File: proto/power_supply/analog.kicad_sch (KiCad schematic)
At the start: 28 parts, among them U401 TSV914, U409 TSV914

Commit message: Finish alim sch, start PCB
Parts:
- renumbered U409 to U401, U401 to U402
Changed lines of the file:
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@@
   (symbol (lib_id "Amplifier_Operational:TSV914") (at 49.53 114.3 0) (unit 1)
     (in_bom yes) (on_board yes) (dnp no) (fields_autoplaced)
-    (property "Reference" "U409" (at 49.53 105.41 0)
+    (property "Reference" "U401" (at 49.53 105.41 0)
       (effects (font (size 1.27 1.27)))
     )
@@
       (project "power_supply"
         (path "/e87df9ac-84db-475c-955a-f1fa477bbb69/9874073e-3ac1-4f88-b38b-85e528930503"
-          (reference "U409") (unit 1)
+          (reference "U401") (unit 1)
         )
       )
@@
   (symbol (lib_id "Amplifier_Operational:TSV914") (at 100.33 114.3 0) (unit 4)
     (in_bom yes) (on_board yes) (dnp no)
-    (property "Reference" "U409" (at 100.33 104.775 0)
+    (property "Reference" "U401" (at 100.33 104.775 0)
       (effects (font (size 1.27 1.27)))
     )
@@
       (project "power_supply"
         (path "/e87df9ac-84db-475c-955a-f1fa477bbb69/9874073e-3ac1-4f88-b38b-85e528930503"
-          (reference "U409") (unit 4)
+          (reference "U401") (unit 4)
         )
       )
@@
   (symbol (lib_id "Amplifier_Operational:TSV914") (at 187.96 114.3 0) (unit 2)
     (in_bom yes) (on_board yes) (dnp no) (fields_autoplaced)
-    (property "Reference" "U401" (at 187.96 105.41 0)
+    (property "Reference" "U402" (at 187.96 105.41 0)
       (effects (font (size 1.27 1.27)))
     )
@@
       (project "power_supply"
         (path "/e87df9ac-84db-475c-955a-f1fa477bbb69/9874073e-3ac1-4f88-b38b-85e528930503"
-          (reference "U401") (unit 2)
+          (reference "U402") (unit 2)
         )
       )
@@
         )
         (path "/e87df9ac-84db-475c-955a-f1fa477bbb69/9874073e-3ac1-4f88-b38b-85e528930503"
-          (reference "C412") (unit 1)
+          (reference "C406") (unit 1)
         )
       )
@@
         )
         (path "/e87df9ac-84db-475c-955a-f1fa477bbb69/9874073e-3ac1-4f88-b38b-85e528930503"
-          (reference "#PWR0438") (unit 1)
+          (reference "#PWR0406") (unit 1)
         )
       )
@@
         )
         (path "/e87df9ac-84db-475c-955a-f1fa477bbb69/9874073e-3ac1-4f88-b38b-85e528930503"
-          (reference "C415") (unit 1)
+          (reference "C407") (unit 1)
         )
       )
@@
         )
         (path "/e87df9ac-84db-475c-955a-f1fa477bbb69/9874073e-3ac1-4f88-b38b-85e528930503"
-          (reference "#PWR0440") (unit 1)
+          (reference "#PWR0408") (unit 1)
         )
       )
@@
         )
         (path "/e87df9ac-84db-475c-955a-f1fa477bbb69/9874073e-3ac1-4f88-b38b-85e528930503"
-          (reference "#PWR0118") (unit 1)
+          (reference "#PWR0410") (unit 1)
         )
       )
@@
   (symbol (lib_id "Amplifier_Operational:TSV914") (at 46.99 44.45 0) (unit 2)
     (in_bom yes) (on_board yes) (dnp no) (fields_autoplaced)
-    (property "Reference" "U409" (at 46.99 34.925 0)
+    (property "Reference" "U401" (at 46.99 34.925 0)
       (effects (font (size 1.27 1.27)))
     )
@@
       (project "power_supply"
         (path "/e87df9ac-84db-475c-955a-f1fa477bbb69/9874073e-3ac1-4f88-b38b-85e528930503"
-          (reference "U409") (unit 2)
+          (reference "U401") (unit 2)
         )
       )
@@
         )
         (path "/e87df9ac-84db-475c-955a-f1fa477bbb69/9874073e-3ac1-4f88-b38b-85e528930503"
-          (reference "#PWR0435") (unit 1)
+          (reference "#PWR0412") (unit 1)
         )
       )
@@
         )
         (path "/e87df9ac-84db-475c-955a-f1fa477bbb69/9874073e-3ac1-4f88-b38b-85e528930503"
-          (reference "C403") (unit 1)
+          (reference "C401") (unit 1)
         )
       )
@@
         )
         (path "/e87df9ac-84db-475c-955a-f1fa477bbb69/9874073e-3ac1-4f88-b38b-85e528930503"
-          (reference "#PWR0417") (unit 1)
+          (reference "#PWR0402") (unit 1)
         )
       )
@@
   (symbol (lib_id "Amplifier_Operational:TSV914") (at 157.48 152.4 0) (unit 5)
     (in_bom yes) (on_board yes) (dnp no) (fields_autoplaced)
-    (property "Reference" "U401" (at 155.575 151.765 0)
+    (property "Reference" "U402" (at 155.575 151.765 0)
       (effects (font (size 1.27 1.27)) (justify left))
     )
@@
       (project "power_supply"
         (path "/e87df9ac-84db-475c-955a-f1fa477bbb69/9874073e-3ac1-4f88-b38b-85e528930503"
-          (reference "U401") (unit 5)
+          (reference "U402") (unit 5)
         )
       )
@@
         )
         (path "/e87df9ac-84db-475c-955a-f1fa477bbb69/9874073e-3ac1-4f88-b38b-85e528930503"
-          (reference "C404") (unit 1)
+          (reference "C402") (unit 1)
         )
       )
@@
   (symbol (lib_id "Amplifier_Operational:TSV914") (at 34.29 157.48 0) (unit 5)
     (in_bom yes) (on_board yes) (dnp no) (fields_autoplaced)
-    (property "Reference" "U409" (at 32.385 156.845 0)
+    (property "Reference" "U401" (at 32.385 156.845 0)
       (effects (font (size 1.27 1.27)) (justify left))
     )
@@
       (project "power_supply"
         (path "/e87df9ac-84db-475c-955a-f1fa477bbb69/9874073e-3ac1-4f88-b38b-85e528930503"
-          (reference "U409") (unit 5)
+          (reference "U401") (unit 5)
         )
       )
@@
         )
         (path "/e87df9ac-84db-475c-955a-f1fa477bbb69/9874073e-3ac1-4f88-b38b-85e528930503"
-          (reference "C411") (unit 1)
+          (reference "C409") (unit 1)
         )
       )
@@
   (symbol (lib_id "Amplifier_Operational:TSV914") (at 177.8 45.72 0) (unit 1)
     (in_bom yes) (on_board yes) (dnp no) (fields_autoplaced)
-    (property "Reference" "U401" (at 177.8 36.83 0)
+    (property "Reference" "U402" (at 177.8 36.83 0)
       (effects (font (size 1.27 1.27)))
     )
@@
       (project "power_supply"
         (path "/e87df9ac-84db-475c-955a-f1fa477bbb69/9874073e-3ac1-4f88-b38b-85e528930503"
-          (reference "U401") (unit 1)
+          (reference "U402") (unit 1)
         )
       )
@@
         )
         (path "/e87df9ac-84db-475c-955a-f1fa477bbb69/9874073e-3ac1-4f88-b38b-85e528930503"
-          (reference "C406") (unit 1)
+          (reference "C404") (unit 1)
         )
       )
@@
         )
         (path "/e87df9ac-84db-475c-955a-f1fa477bbb69/9874073e-3ac1-4f88-b38b-85e528930503"
-          (reference "C410") (unit 1)
+          (reference "C405") (unit 1)
         )
       )
@@
         )
         (path "/e87df9ac-84db-475c-955a-f1fa477bbb69/9874073e-3ac1-4f88-b38b-85e528930503"
-          (reference "#PWR0437") (unit 1)
+          (reference "#PWR0405") (unit 1)
         )
       )
@@
         )
         (path "/e87df9ac-84db-475c-955a-f1fa477bbb69/9874073e-3ac1-4f88-b38b-85e528930503"
-          (reference "#PWR0439") (unit 1)
+          (reference "#PWR0407") (unit 1)
         )
       )
@@
   (symbol (lib_id "Amplifier_Operational:TSV914") (at 238.76 114.3 0) (unit 3)
     (in_bom yes) (on_board yes) (dnp no) (fields_autoplaced)
-    (property "Reference" "U401" (at 238.76 105.41 0)
+    (property "Reference" "U402" (at 238.76 105.41 0)
       (effects (font (size 1.27 1.27)))
     )
@@
       (project "power_supply"
         (path "/e87df9ac-84db-475c-955a-f1fa477bbb69/9874073e-3ac1-4f88-b38b-85e528930503"
-          (reference "U401") (unit 3)
+          (reference "U402") (unit 3)
         )
       )
@@
         )
         (path "/e87df9ac-84db-475c-955a-f1fa477bbb69/9874073e-3ac1-4f88-b38b-85e528930503"
-          (reference "C416") (unit 1)
+          (reference "C408") (unit 1)
         )
       )
@@
         )
         (path "/e87df9ac-84db-475c-955a-f1fa477bbb69/9874073e-3ac1-4f88-b38b-85e528930503"
-          (reference "#PWR0419") (unit 1)
+          (reference "#PWR0403") (unit 1)
         )
       )
@@
         )
         (path "/e87df9ac-84db-475c-955a-f1fa477bbb69/9874073e-3ac1-4f88-b38b-85e528930503"
-          (reference "#PWR0124") (unit 1)
+          (reference "#PWR0409") (unit 1)
         )
       )
@@
   (symbol (lib_id "Amplifier_Operational:TSV914") (at 114.3 49.53 0) (unit 3)
     (in_bom yes) (on_board yes) (dnp no) (fields_autoplaced)
-    (property "Reference" "U409" (at 114.3 40.005 0)
+    (property "Reference" "U401" (at 114.3 40.005 0)
       (effects (font (size 1.27 1.27)))
     )
@@
       (project "power_supply"
         (path "/e87df9ac-84db-475c-955a-f1fa477bbb69/9874073e-3ac1-4f88-b38b-85e528930503"
-          (reference "U409") (unit 3)
+          (reference "U401") (unit 3)
         )
       )
@@
         )
         (path "/e87df9ac-84db-475c-955a-f1fa477bbb69/9874073e-3ac1-4f88-b38b-85e528930503"
-          (reference "#PWR0415") (unit 1)
+          (reference "#PWR0401") (unit 1)
         )
       )
@@
         )
         (path "/e87df9ac-84db-475c-955a-f1fa477bbb69/9874073e-3ac1-4f88-b38b-85e528930503"
-          (reference "C413") (unit 1)
+          (reference "C410") (unit 1)
         )
       )
@@
         )
         (path "/e87df9ac-84db-475c-955a-f1fa477bbb69/9874073e-3ac1-4f88-b38b-85e528930503"
-          (reference "C405") (unit 1)
+          (reference "C403") (unit 1)
         )
       )
@@
   (symbol (lib_id "Amplifier_Operational:TSV914") (at 245.11 50.8 0) (unit 4)
     (in_bom yes) (on_board yes) (dnp no) (fields_autoplaced)
-    (property "Reference" "U401" (at 245.11 41.91 0)
+    (property "Reference" "U402" (at 245.11 41.91 0)
       (effects (font (size 1.27 1.27)))
     )
@@
       (project "power_supply"
         (path "/e87df9ac-84db-475c-955a-f1fa477bbb69/9874073e-3ac1-4f88-b38b-85e528930503"
-          (reference "U401") (unit 4)
+          (reference "U402") (unit 4)
         )
       )
@@
         )
         (path "/e87df9ac-84db-475c-955a-f1fa477bbb69/9874073e-3ac1-4f88-b38b-85e528930503"
-          (reference "#PWR0424") (unit 1)
+          (reference "#PWR0411") (unit 1)
         )
       )
@@
         )
         (path "/e87df9ac-84db-475c-955a-f1fa477bbb69/9874073e-3ac1-4f88-b38b-85e528930503"
-          (reference "#PWR0420") (unit 1)
-        )
-      )
+          (reference "#PWR0404") (unit 1)
+        )
+      )

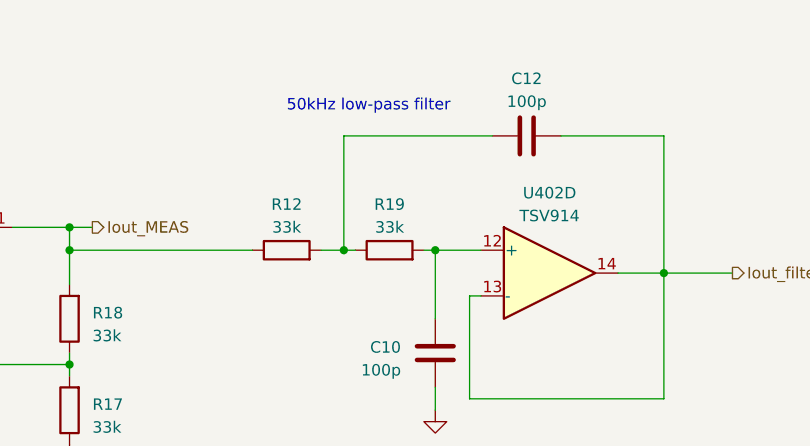
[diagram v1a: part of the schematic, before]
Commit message: Finish first routing
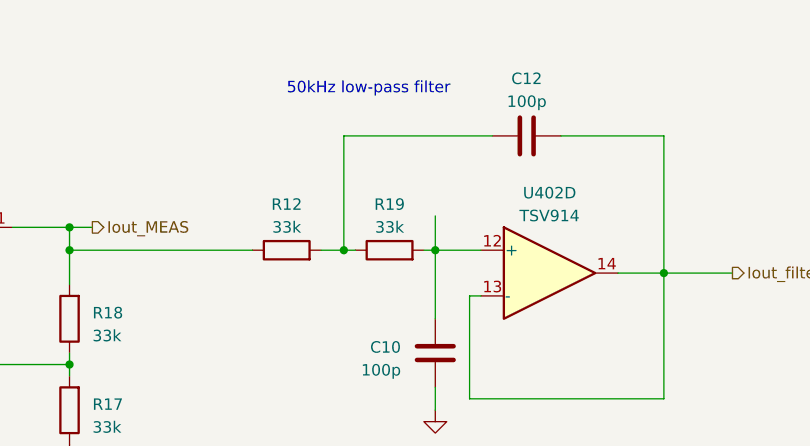
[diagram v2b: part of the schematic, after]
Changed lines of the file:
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@@
+    (stroke (width 0) (type default))
+  )
+  (wire (pts (xy 232.41 44.45) (xy 232.41 48.26))
     (stroke (width 0) (type default))
   )
@@
     (effects (font (size 1.27 1.27)) (justify left bottom))
   )
-  (text "50kHz low-pass filter" (at 215.9 33.02 0)
+  (text "50kHz low-pass filter" (at 215.9 31.115 0)
     (effects (font (size 1.27 1.27)) (justify left bottom))
   )
@@
     )
   )
+  (netclass_flag "" (length 2.54) (shape round) (at 222.25 35.56 0) (fields_autoplaced)
+    (effects (font (size 1.27 1.27)) (justify left bottom))
+    (property "Netclass" "Analog" (at 223.139 33.02 0)
+      (effects (font (size 1.27 1.27) italic) (justify left))
+    )
+  )
   (netclass_flag "" (length 2.54) (shape round) (at 93.345 34.29 0) (fields_autoplaced)
     (effects (font (size 1.27 1.27)) (justify left bottom))
     (property "Netclass" "Analog" (at 94.234 31.75 0)
+      (effects (font (size 1.27 1.27) italic) (justify left))
+    )
+  )
+  (netclass_flag "" (length 2.54) (shape round) (at 232.41 44.45 0) (fields_autoplaced)
+    (effects (font (size 1.27 1.27)) (justify left bottom))
+    (property "Netclass" "Analog" (at 233.299 41.91 0)
       (effects (font (size 1.27 1.27) italic) (justify left))
     )
@@
       (effects (font (size 1.27 1.27) italic) (justify left))
     )
+  )
+  (netclass_flag "" (length 2.54) (shape round) (at 177.8 60.96 0) (fields_autoplaced)
+    (effects (font (size 1.27 1.27)) (justify left bottom))
+    (property "Netclass" "Analog" (at 178.689 58.42 0)
+      (effects (font (size 1.27 1.27) italic) (justify left))
+    )
